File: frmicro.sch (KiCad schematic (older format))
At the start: 14 parts

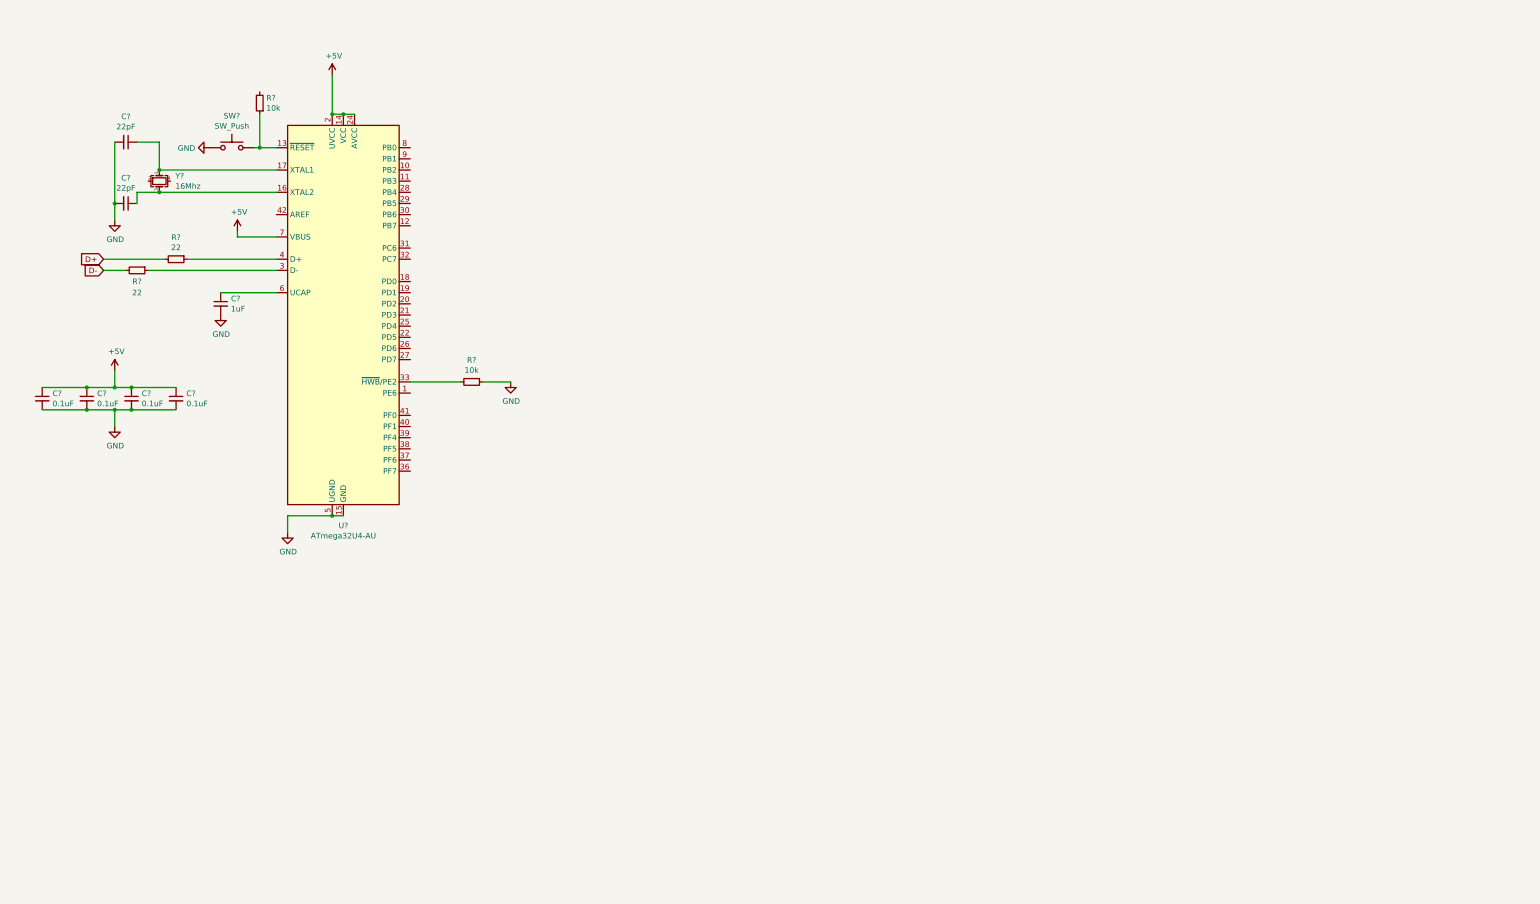
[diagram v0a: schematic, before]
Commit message: add usb-c 2.0 connector
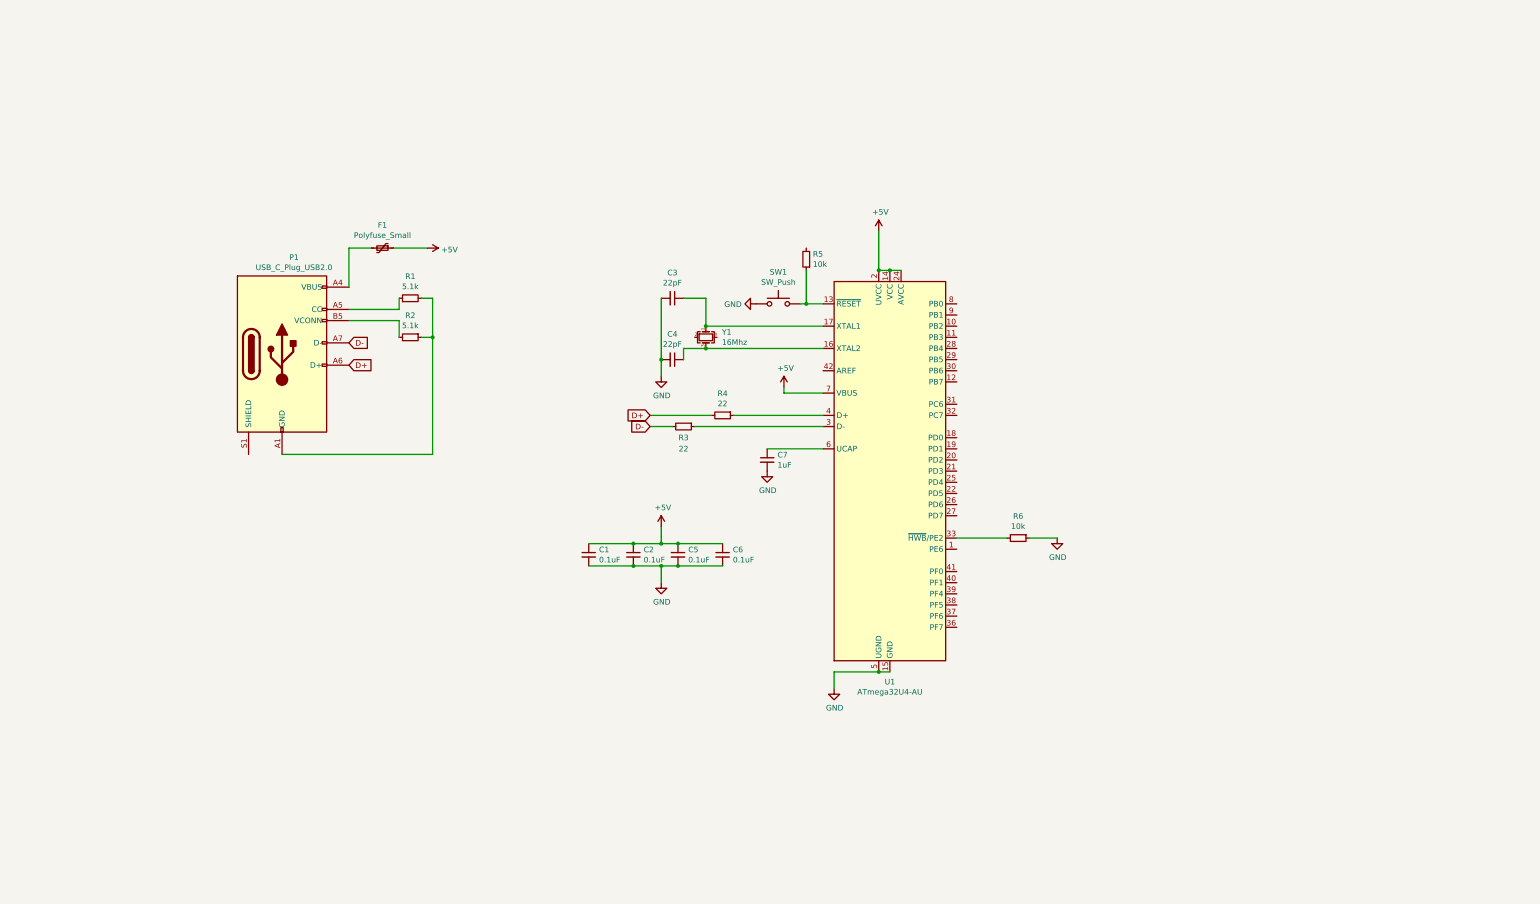
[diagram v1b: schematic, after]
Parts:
- added F1: Polyfuse_Small, symbol Device:Polyfuse_Small
- added P1: USB_C_Plug_USB2.0, symbol Connector:USB_C_Plug_USB2.0
- added R1, R2: 5.1k, symbol Device:R_Small
- gave numbers to parts that had none: 14
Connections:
- net +5V: now also F1.1
- net D+: now also P1.A6 (D+)
- net D-: now also P1.A7 (D-)
- new net: P1.A1 (GND), P1.A12 (GND), P1.B1 (GND), P1.B12 (GND), R1.2, R2.1
- new net: F1.2, P1.A4 (VBUS), P1.A9 (VBUS), P1.B4 (VBUS), P1.B9 (VBUS)
- new net: P1.A5 (CC), R1.1
- new net: P1.B5 (VCONN), R2.2
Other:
- moved on the sheet: C1, C2, C3, C4, C5, C6, C7, R3, R4, R5, R6, SW1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

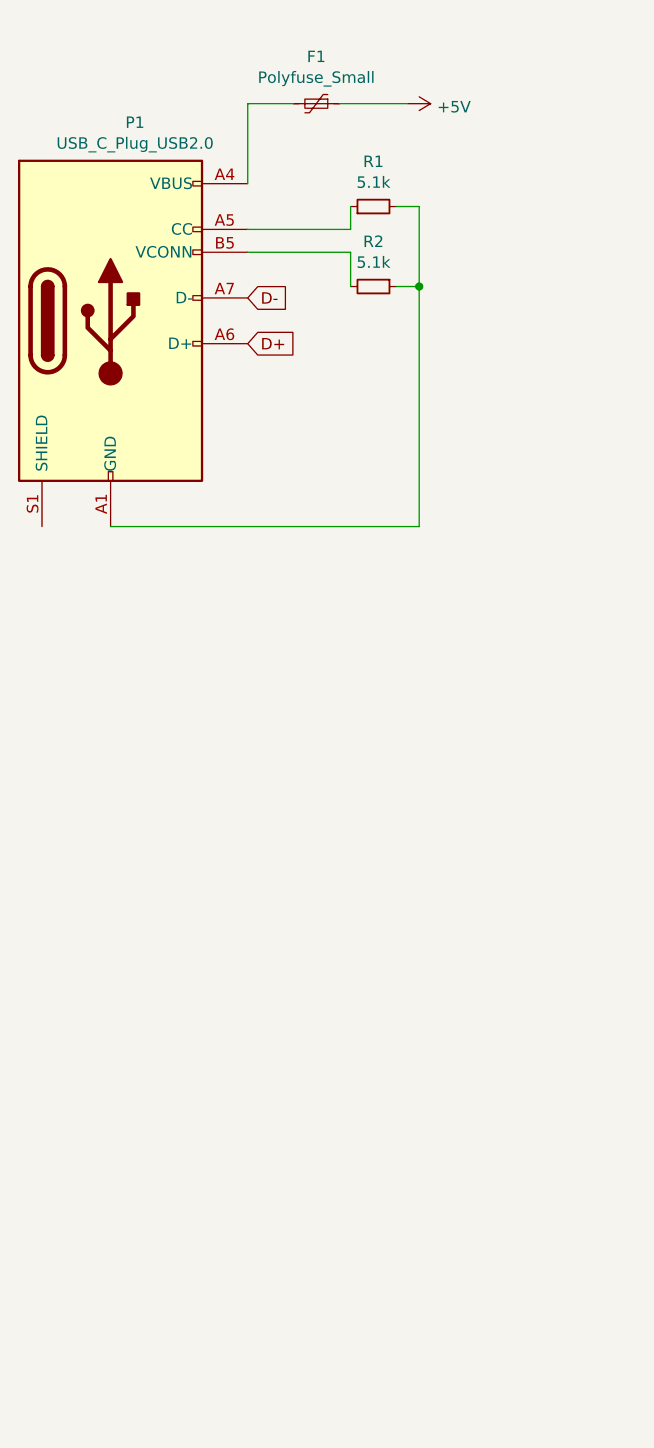
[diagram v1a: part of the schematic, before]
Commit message: add pcb footprints and add links to readme
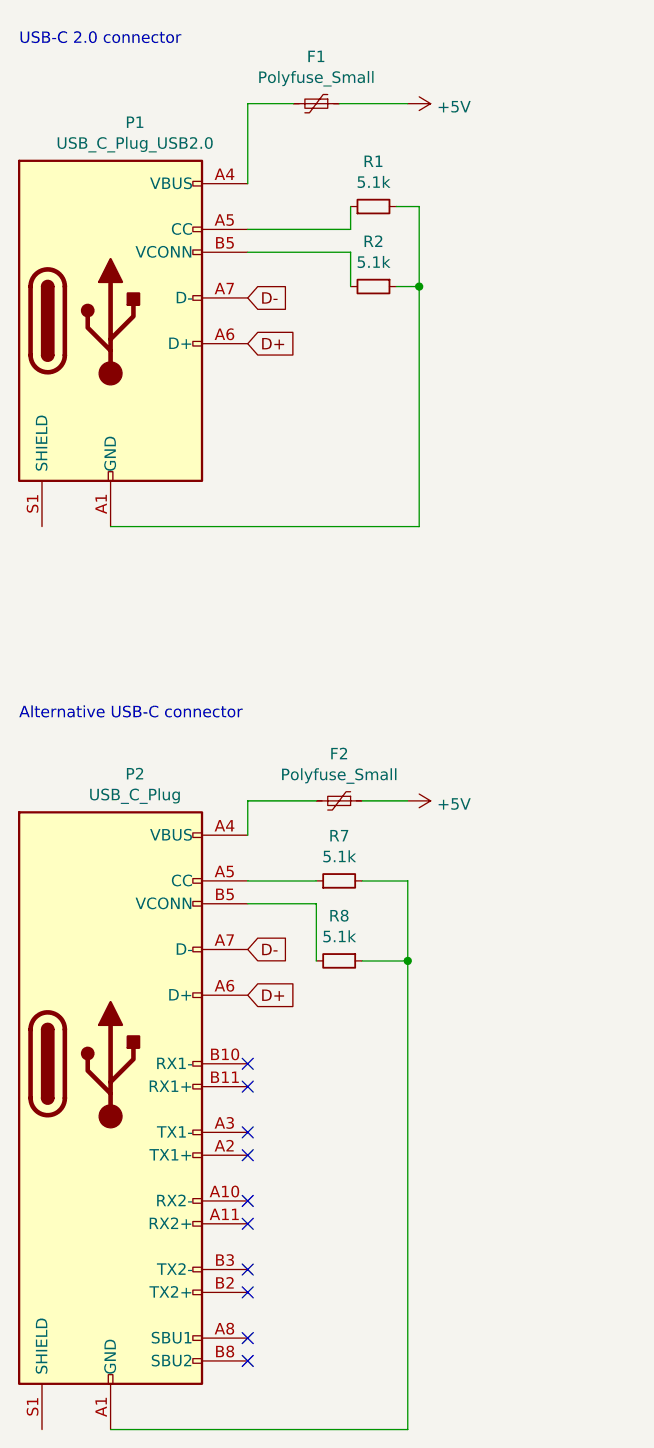
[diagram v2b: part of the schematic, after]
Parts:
- added F2: Polyfuse_Small, Fuse:Fuse_0805_2012Metric, symbol Device:Polyfuse_Small
- added P2: USB_C_Plug, Connector_USB:USB_C_Plug_JAE_DX07P024AJ1, symbol Connector:USB_C_Plug
- added R7, R8: 5.1k, Resistor_SMD:R_0805_2012Metric, symbol Device:R_Small
- C1, C2, C3, C4, C5, C6, C7: footprint (none) -> Capacitor_SMD:C_0805_2012Metric
- F1: footprint (none) -> Fuse:Fuse_0805_2012Metric
- P1: footprint (none) -> Connector_USB:USB_C_Plug_JAE_DX07P024AJ1
- R1, R2, R3, R4, R5, R6: footprint (none) -> Resistor_SMD:R_0805_2012Metric
- SW1: footprint (none) -> misc:SW_PTS636_SM43J_SMTR_LFS
- Y1: footprint (none) -> Crystal:Crystal_SMD_3225-4Pin_3.2x2.5mm
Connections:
- net +5V: now also F2.1
- net D+: now also P2.A6 (D+)
- net D-: now also P2.A7 (D-)
- new net: P2.A1 (GND), P2.A12 (GND), P2.B1 (GND), P2.B12 (GND), R7.2, R8.1
- new net: F2.2, P2.A4 (VBUS), P2.A9 (VBUS), P2.B4 (VBUS), P2.B9 (VBUS)
- new net: P2.A5 (CC), R7.1
- new net: P2.B5 (VCONN), R8.2
- no-connect marks 0 -> 10
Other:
- note added: "Alternative USB-C connector"
- note added: "USB-C 2.0 connector"
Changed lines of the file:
@@
 F 0 "R6" V 10154 5650 50  0000 C CNN
 F 1 "10k" V 10245 5650 50  0000 C CNN
-F 2 "" H 10350 5650 50  0001 C CNN
+F 2 "Resistor_SMD:R_0805_2012Metric" H 10350 5650 50  0001 C CNN
 F 3 "~" H 10350 5650 50  0001 C CNN
 	1    10350 5650
@@
 F 0 "R4" V 7504 4550 50  0000 C CNN
 F 1 "22" V 7595 4550 50  0000 C CNN
-F 2 "" H 7700 4550 50  0001 C CNN
+F 2 "Resistor_SMD:R_0805_2012Metric" H 7700 4550 50  0001 C CNN
 F 3 "~" H 7700 4550 50  0001 C CNN
 	1    7700 4550
@@
 F 0 "R3" V 7450 4650 50  0000 C CNN
 F 1 "22" V 7550 4650 50  0000 C CNN
-F 2 "" H 7350 4650 50  0001 C CNN
+F 2 "Resistor_SMD:R_0805_2012Metric" H 7350 4650 50  0001 C CNN
 F 3 "~" H 7350 4650 50  0001 C CNN
 	1    7350 4650
@@
 F 0 "C7" H 8192 4996 50  0000 L CNN
 F 1 "1uF" H 8192 4905 50  0000 L CNN
-F 2 "" H 8100 4950 50  0001 C CNN
+F 2 "Capacitor_SMD:C_0805_2012Metric" H 8100 4950 50  0001 C CNN
 F 3 "~" H 8100 4950 50  0001 C CNN
 	1    8100 4950
@@
 F 0 "C5" H 7392 5846 50  0000 L CNN
 F 1 "0.1uF" H 7392 5755 50  0000 L CNN
-F 2 "" H 7300 5800 50  0001 C CNN
+F 2 "Capacitor_SMD:C_0805_2012Metric" H 7300 5800 50  0001 C CNN
 F 3 "~" H 7300 5800 50  0001 C CNN
 	1    7300 5800
@@
 F 0 "C6" H 7792 5846 50  0000 L CNN
 F 1 "0.1uF" H 7792 5755 50  0000 L CNN
-F 2 "" H 7700 5800 50  0001 C CNN
+F 2 "Capacitor_SMD:C_0805_2012Metric" H 7700 5800 50  0001 C CNN
 F 3 "~" H 7700 5800 50  0001 C CNN
 	1    7700 5800
@@
 F 0 "C2" H 6992 5846 50  0000 L CNN
 F 1 "0.1uF" H 6992 5755 50  0000 L CNN
-F 2 "" H 6900 5800 50  0001 C CNN
+F 2 "Capacitor_SMD:C_0805_2012Metric" H 6900 5800 50  0001 C CNN
 F 3 "~" H 6900 5800 50  0001 C CNN
 	1    6900 5800
@@
 F 0 "C1" H 6592 5846 50  0000 L CNN
 F 1 "0.1uF" H 6592 5755 50  0000 L CNN
-F 2 "" H 6500 5800 50  0001 C CNN
+F 2 "Capacitor_SMD:C_0805_2012Metric" H 6500 5800 50  0001 C CNN
 F 3 "~" H 6500 5800 50  0001 C CNN
 	1    6500 5800
@@
 F 0 "Y1" V 7504 3994 50  0000 L CNN
 F 1 "16Mhz" V 7595 3994 50  0000 L CNN
-F 2 "" H 7550 3850 50  0001 C CNN
+F 2 "Crystal:Crystal_SMD_3225-4Pin_3.2x2.5mm" H 7550 3850 50  0001 C CNN
 F 3 "~" H 7550 3850 50  0001 C CNN
 	1    7550 3850
@@
 F 0 "C3" V 7021 3500 50  0000 C CNN
 F 1 "22pF" V 7112 3500 50  0000 C CNN
-F 2 "" H 7250 3500 50  0001 C CNN
+F 2 "Capacitor_SMD:C_0805_2012Metric" H 7250 3500 50  0001 C CNN
 F 3 "~" H 7250 3500 50  0001 C CNN
 	1    7250 3500
@@
 F 0 "C4" V 7021 4050 50  0000 C CNN
 F 1 "22pF" V 7112 4050 50  0000 C CNN
-F 2 "" H 7250 4050 50  0001 C CNN
+F 2 "Capacitor_SMD:C_0805_2012Metric" H 7250 4050 50  0001 C CNN
 F 3 "~" H 7250 4050 50  0001 C CNN
 	1    7250 4050
@@
 F 0 "SW1" H 8200 3835 50  0000 C CNN
 F 1 "SW_Push" H 8200 3744 50  0000 C CNN
-F 2 "" H 8200 3750 50  0001 C CNN
+F 2 "misc:SW_PTS636_SM43J_SMTR_LFS" H 8200 3750 50  0001 C CNN
 F 3 "~" H 8200 3750 50  0001 C CNN
 	1    8200 3550
@@
 F 0 "R5" H 8391 3104 50  0000 R CNN
 F 1 "10k" H 8391 3195 50  0000 R CNN
-F 2 "" H 8450 3150 50  0001 C CNN
+F 2 "Resistor_SMD:R_0805_2012Metric" H 8450 3150 50  0001 C CNN
 F 3 "~" H 8450 3150 50  0001 C CNN
 	1    8450 3150
@@
 F 0 "P1" H 3857 4867 50  0000 C CNN
 F 1 "USB_C_Plug_USB2.0" H 3857 4776 50  0000 C CNN
-F 2 "" H 3900 4000 50  0001 C CNN
+F 2 "Connector_USB:USB_C_Plug_JAE_DX07P024AJ1" H 3900 4000 50  0001 C CNN
 F 3 "https://www.usb.org/sites/default/files/documents/usb_type-c.zip" H 3900 4000 50  0001 C CNN
 	1    3750 4000
@@
 F 0 "R1" V 5096 3500 50  0000 C CNN
 F 1 "5.1k" V 5005 3500 50  0000 C CNN
-F 2 "" H 4900 3500 50  0001 C CNN
+F 2 "Resistor_SMD:R_0805_2012Metric" H 4900 3500 50  0001 C CNN
 F 3 "~" H 4900 3500 50  0001 C CNN
 	1    4900 3500
@@
 F 0 "R2" V 4704 3850 50  0000 C CNN
 F 1 "5.1k" V 4795 3850 50  0000 C CNN
-F 2 "" H 4900 3850 50  0001 C CNN
+F 2 "Resistor_SMD:R_0805_2012Metric" H 4900 3850 50  0001 C CNN
 F 3 "~" H 4900 3850 50  0001 C CNN
 	1    4900 3850
@@
 F 0 "F1" V 4445 3050 50  0000 C CNN
 F 1 "Polyfuse_Small" V 4536 3050 50  0000 C CNN
-F 2 "" H 4700 2850 50  0001 L CNN
+F 2 "Fuse:Fuse_0805_2012Metric" H 4700 2850 50  0001 L CNN
 F 3 "~" H 4650 3050 50  0001 C CNN
 	1    4650 3050
@@
 Wire Wire Line
 	5100 3850 5100 4900
+$Comp
+L Connector:USB_C_Plug P2
+U 1 1 615B98A9
+P 3750 7250
+F 0 "P2" H 3857 8517 50  0000 C CNN
+F 1 "USB_C_Plug" H 3857 8426 50  0000 C CNN
+F 2 "Connector_USB:USB_C_Plug_JAE_DX07P024AJ1" H 3900 7250 50  0001 C CNN
+F 3 "https://www.usb.org/sites/default/files/documents/usb_type-c.zip" H 3900 7250 50  0001 C CNN
+	1    3750 7250
+	1    0    0    -1
+$EndComp
+$Comp
+L Device:Polyfuse_Small F2
+U 1 1 615BD138
+P 4750 6100
+F 0 "F2" V 4545 6100 50  0000 C CNN
+F 1 "Polyfuse_Small" V 4636 6100 50  0000 C CNN
+F 2 "Fuse:Fuse_0805_2012Metric" H 4800 5900 50  0001 L CNN
+F 3 "~" H 4750 6100 50  0001 C CNN
+	1    4750 6100
+	0    1    1    0
+$EndComp
+$Comp
+L power:+5V #PWR011
+U 1 1 615BDB31
+P 5050 6100
+F 0 "#PWR011" H 5050 5950 50  0001 C CNN
+F 1 "+5V" V 5065 6228 50  0000 L CNN
+F 2 "" H 5050 6100 50  0001 C CNN
+F 3 "" H 5050 6100 50  0001 C CNN
+	1    5050 6100
+	0    1    1    0
+$EndComp
+Wire Wire Line
+	4350 6250 4350 6100
+Wire Wire Line
+	4350 6100 4650 6100
+Wire Wire Line
+	4850 6100 5050 6100
+$Comp
+L Device:R_Small R7
+U 1 1 615BF709
+P 4750 6450
+F 0 "R7" V 4946 6450 50  0000 C CNN
+F 1 "5.1k" V 4855 6450 50  0000 C CNN
+F 2 "Resistor_SMD:R_0805_2012Metric" H 4750 6450 50  0001 C CNN
+F 3 "~" H 4750 6450 50  0001 C CNN
+	1    4750 6450
+	0    -1   -1   0
+$EndComp
+$Comp
+L Device:R_Small R8
+U 1 1 615BFC60
+P 4750 6800
+F 0 "R8" V 4554 6800 50  0000 C CNN
+F 1 "5.1k" V 4645 6800 50  0000 C CNN
+F 2 "Resistor_SMD:R_0805_2012Metric" H 4750 6800 50  0001 C CNN
+F 3 "~" H 4750 6800 50  0001 C CNN
+	1    4750 6800
+	0    1    1    0
+$EndComp
+Wire Wire Line
+	4350 6450 4650 6450
+Wire Wire Line
+	5050 6450 5050 6800
+Wire Wire Line
+	5050 8850 3750 8850
+Wire Wire Line
+	4850 6450 5050 6450
+Wire Wire Line
+	4350 6550 4650 6550
+Wire Wire Line
+	4650 6550 4650 6800
+Wire Wire Line
+	5050 6800 4850 6800
+Connection ~ 5050 6800
+Wire Wire Line
+	5050 6800 5050 8850
+Text GLabel 4350 6750 2    50   Input ~ 0
+D-
+Text GLabel 4350 6950 2    50   Input ~ 0
+D+
+NoConn ~ 4350 7250
+NoConn ~ 4350 7350
+NoConn ~ 4350 7550
+NoConn ~ 4350 7650
+NoConn ~ 4350 7850
+NoConn ~ 4350 7950
+NoConn ~ 4350 8150
+NoConn ~ 4350 8250
+NoConn ~ 4350 8450
+NoConn ~ 4350 8550
+Text Notes 3350 5750 0    50   ~ 0
+Alternative USB-C connector
+Text Notes 3350 2800 0    50   ~ 0
+USB-C 2.0 connector
 $EndSCHEMATC
